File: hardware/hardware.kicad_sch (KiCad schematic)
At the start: 19 parts, among them J1 12V Power Input, M1 AR0959 Motor, M2 AR0959 Motor, M3 AR0959 Motor, U1 Esp32 DevKit, U2 GY-87, U3 TB6612FNG, U4 TB6612FNG

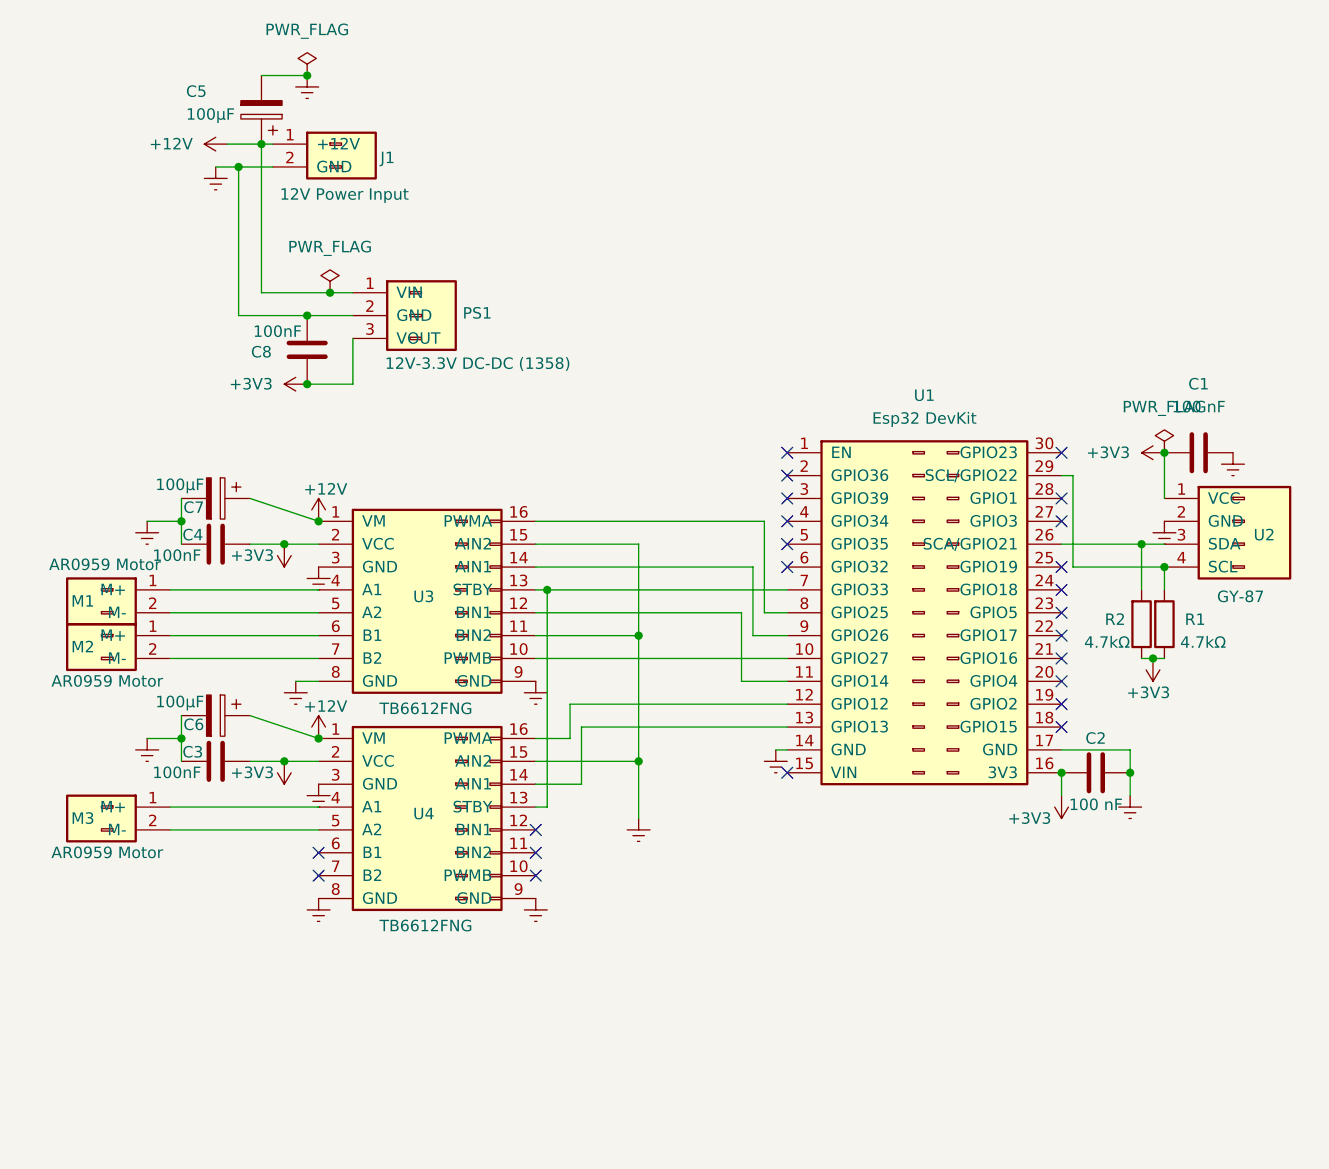
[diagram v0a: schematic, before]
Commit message: new schematic with all planned parts
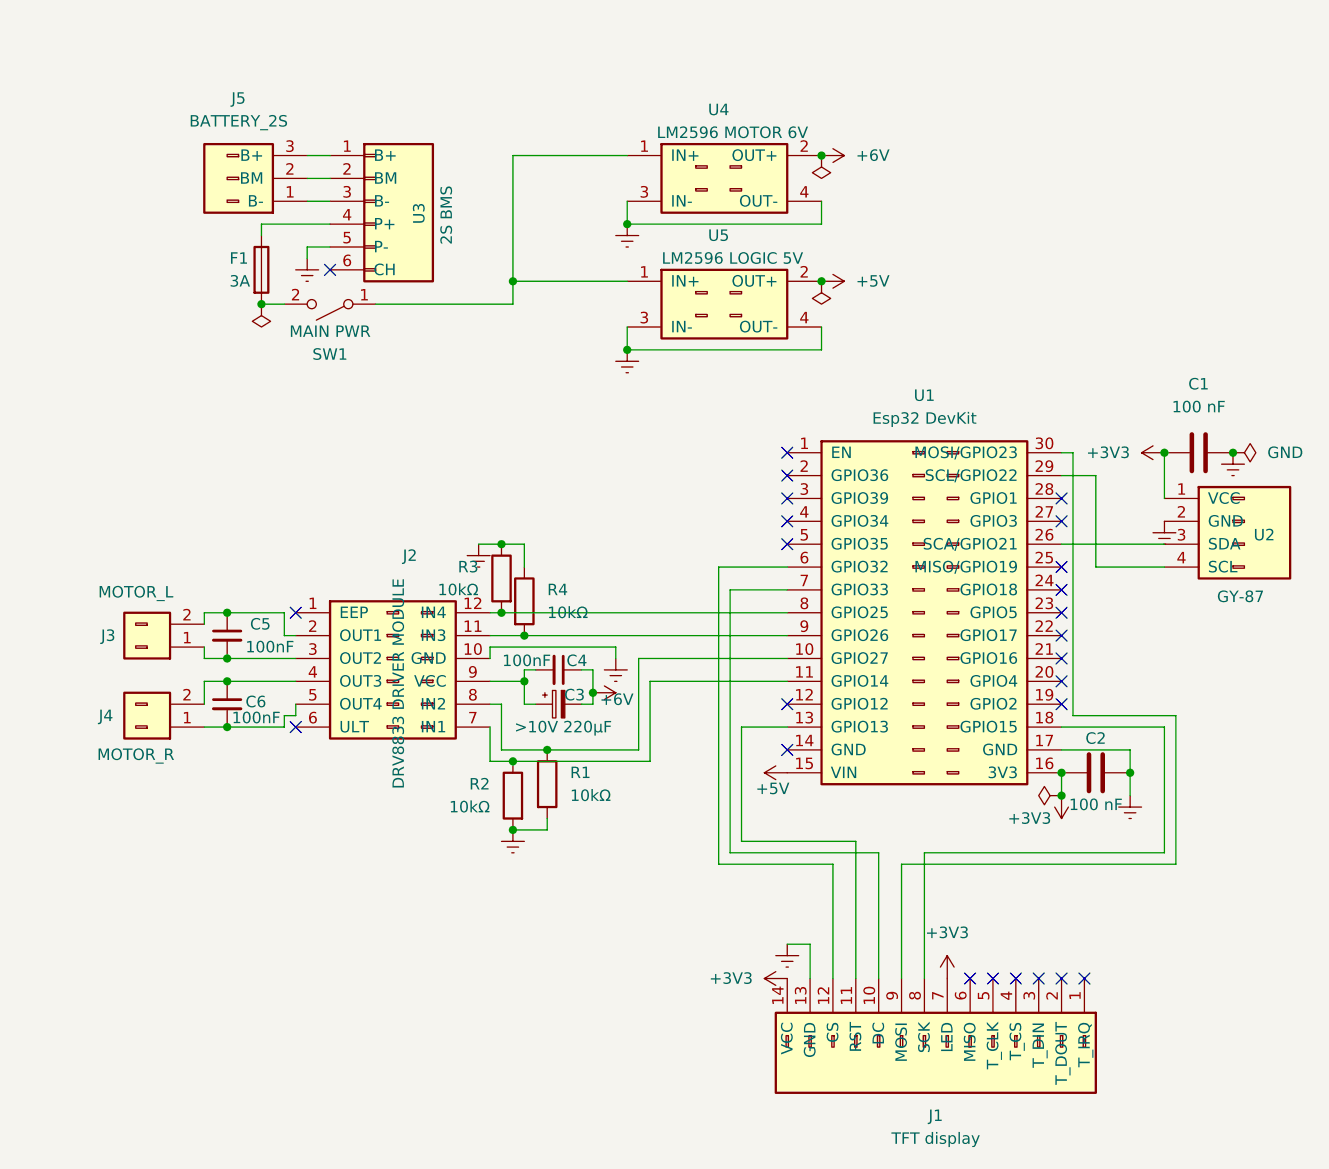
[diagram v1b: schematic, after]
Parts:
- removed C3, C4, C8: 100nF, symbol Device:C
- removed C5, C6, C7: 100μF, symbol Device:C_Polarized
- removed J1: 12V Power Input, PinHeader_1x02_P2.54mm_Vertical, symbol Connector_Generic:Conn_01x02
- removed M1, M2, M3: AR0959 Motor, TerminalBlock_bornier-2_P5.08mm, symbol Connector_Generic:Conn_01x02
- removed PS1: 12V-3.3V DC-DC (1358), PinHeader_1x03_P2.54mm_Vertical, symbol Connector_Generic:Conn_01x03
- removed U3, U4: TB6612FNG, PinHeader_2x08_P2.54mm_Vertical, symbol Connector_Generic:Conn_02x08_Counter_Clockwise
- added C3: >10V 220μF, symbol Device:C_Polarized_Small
- added C4, C5, C6: 100nF, symbol Device:C_Small
- added F1: 3A, symbol Device:Fuse
- added J1: TFT display, symbol Connector_Generic:Conn_01x14
- added J2: DRV8833 DRIVER MODULE, symbol Connector_Generic:Conn_02x06_Counter_Clockwise
- added J3: MOTOR_L, symbol Connector_Generic:Conn_01x02
- added J4: MOTOR_R, symbol Connector_Generic:Conn_01x02
- added J5: BATTERY_2S, symbol Connector_Generic:Conn_01x03
- added R3, R4: 10kΩ, symbol Device:R
- added SW1: MAIN PWR, symbol Switch:SW_SPST
- added U3: 2S BMS, symbol Connector_Generic:Conn_01x06
- added U4: LM2596 MOTOR 6V, symbol Connector_Generic:Conn_02x02_Odd_Even
- added U5: LM2596 LOGIC 5V, symbol Connector_Generic:Conn_02x02_Odd_Even
- R1, R2: value 4.7kΩ -> 10kΩ
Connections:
- net +3V3: now also J1.14 (VCC), J1.7 (LED); no longer R1.1, R2.1
- net GND: now also R1.2, R2.2, J1.13 (GND), J2.10 (GND), R3.1, R4.1, U3.5 (P-), U4.3 (IN-), U4.4 (OUT-), U5.3 (IN-), U5.4 (OUT-); no longer U1.14 (GND)
- net at U1.10 (GPIO27): now also R1.1, J2.8 (IN2)
- net at U1.11 (GPIO14): now also R2.1, J2.7 (IN1)
- net at U1.13 (GPIO13): now also J1.11 (RST)
- net +5V: now reaches U1.15 (VIN)
- net +5V: now also U5.2 (OUT+)
- net at U1.18 (GPIO15): now also J1.8 (SCK)
- net at U1.26 (SCA/GPIO21), U2.3 (SDA): no longer R2.2
- net at U1.29 (SCL/GPIO22), U2.4 (SCL): no longer R1.2
- net at U1.30 (ΜΟSI/GPIO23): now also J1.9 (MOSI)
- net at U1.6 (GPIO32): now also J1.12 (CS)
- net at U1.7 (GPIO33): now also J1.10 (DC)
- net at U1.8 (GPIO25): now also J2.12 (IN4), R3.2
- net at U1.9 (GPIO26): now also J2.11 (IN3), R4.2
- new net: J5.1 (B-), U3.3 (B-)
- new net: J5.2 (BM), U3.2 (BM)
- new net: J5.3 (B+), U3.1 (B+)
- new net: SW1.1 (A), U4.1 (IN+), U5.1 (IN+)
- new net: F1.2, SW1.2 (B)
- new net: C6.1, J2.4 (OUT3), J4.2 (Pin_2)
- new net: C6.2, J2.5 (OUT4), J4.1 (Pin_1)
- new net: C5.1, J2.2 (OUT1), J3.2 (Pin_2)
- new net: C5.2, J2.3 (OUT2), J3.1 (Pin_1)
- new net: C3.1, C4.2, J2.9 (VCC)
- new net: F1.1, U3.4 (P+)
- new net +6V: C3.2, C4.1, U4.2 (OUT+)
- no-connect marks 23 -> 25
